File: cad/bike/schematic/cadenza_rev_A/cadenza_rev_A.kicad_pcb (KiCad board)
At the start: 2 copper layers, 90 x 60 mm, 80 parts, among them J2 USB_C_Receptacle, J3 Conn_01x02, J4 Conn_01x02, J5 Conn_01x02, J7 Conn_01x02, J8 Conn_01x06, Q1 BC547, SW1 SW_Slide_DPDT, SW2 SW_Push, SW3 SW_Push, SW4 SW_Push, U1 TLC5916, U10 HDSP-A151, U11 TLC5916, U12 HDSP-A151, U13 STM32F105RCTx, U14 LT1962-3.3, U15 TLC5916, U2 HDSP-A151, U3 TLC5916, U4 HDSP-A151, U5 TLC5916, U6 HDSP-A151, U7 TLC5916, U8 HDSP-A151, U9 TLC5916

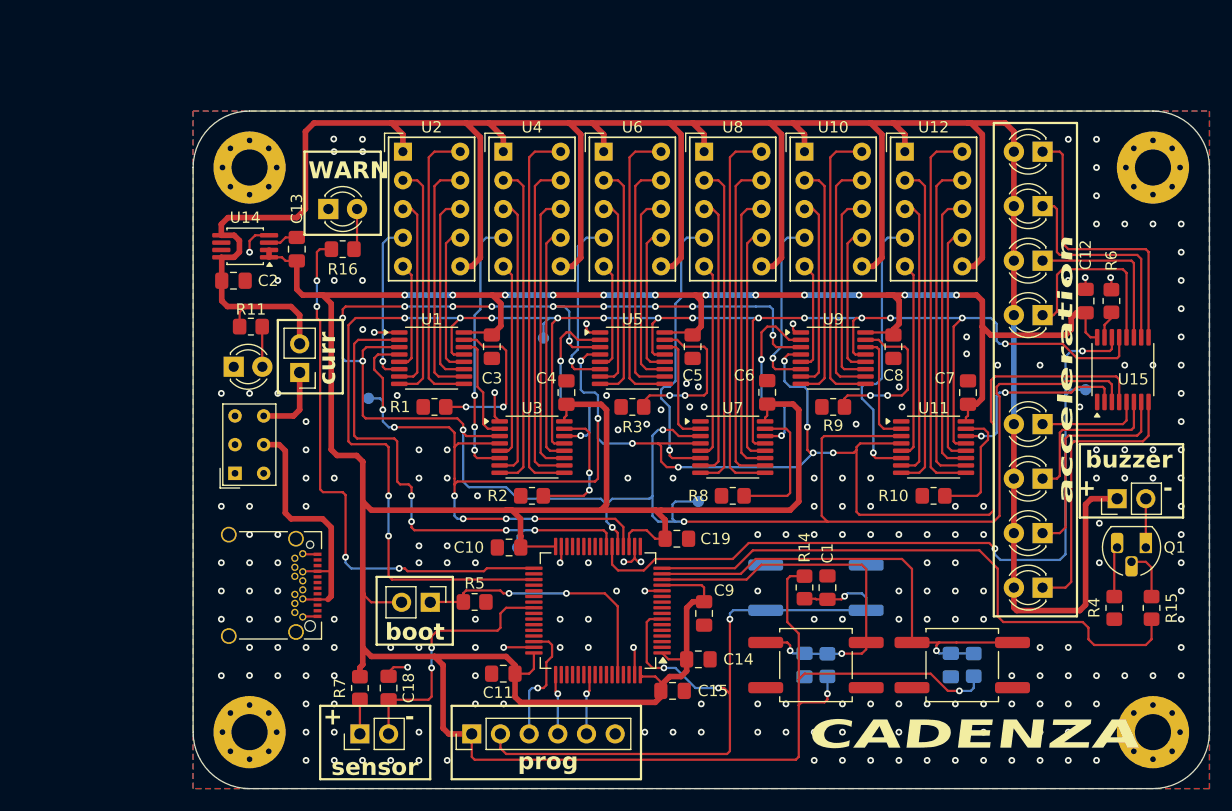
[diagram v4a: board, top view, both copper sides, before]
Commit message: added schematic added software pinout definition
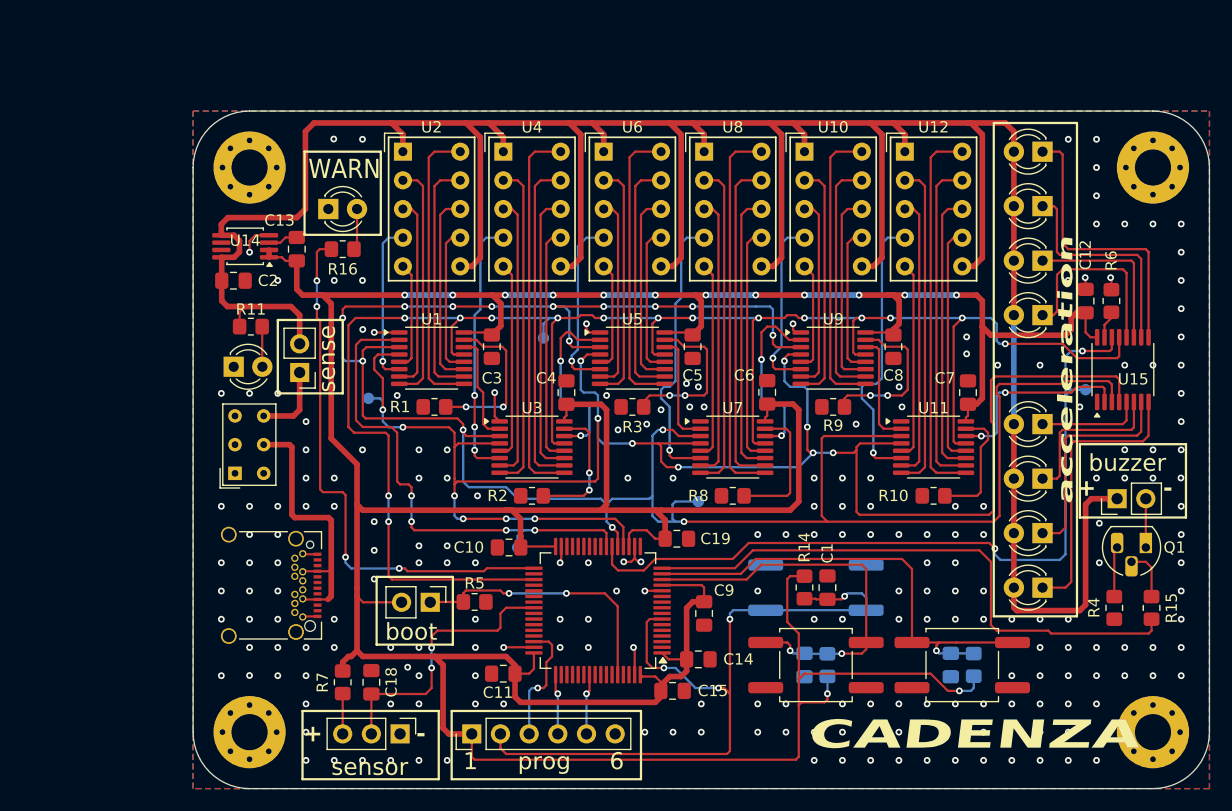
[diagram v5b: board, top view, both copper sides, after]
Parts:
- removed J5: Conn_01x02, Connector_PinHeader_2.54mm:PinHeader_1x02_P2.54mm_Vertical
- added J6: Conn_01x03, Connector_PinHeader_2.54mm:PinHeader_1x03_P2.54mm_Vertical, F.Cu at (68.3, 105.2)
- moved C18 1.61 mm to (65.8, 100.6)
- moved R7 1.61 mm to (63.2, 100.6)
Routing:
- net GND: track 29.2 -> 27.0 mm, vias 214 -> 222
- net Net-(J6-Pin_2): track 23.1 -> 24.5 mm
- net Net-(U13-PA2): track 52.5 -> 51.4 mm
- net /SPI_MOSI: track 45.3 -> 44.5 mm
- net Net-(J2-VBUS-PadA4): track 23.4 -> 24.0 mm
- net Net-(J6-Pin_3): track 3.06 -> 3.57 mm
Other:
- board text added: "1"
- board text added: "6"
- board text added: "sense"
- board text removed: "curr"
